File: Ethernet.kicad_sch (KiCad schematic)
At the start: 37 parts, among them J15 RJ45_Hanrun_HR911105A_Horizon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, U7 LAN8720AI-CP-TR, X3 XL2EL89CSI-111YLC-25M

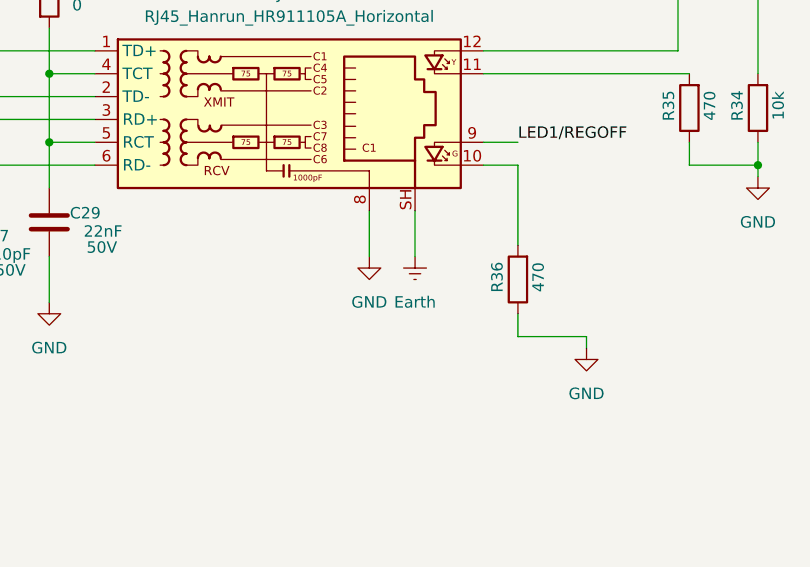
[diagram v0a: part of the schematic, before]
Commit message: Key CHanges for connector choices , termination and semi-final decisions on them
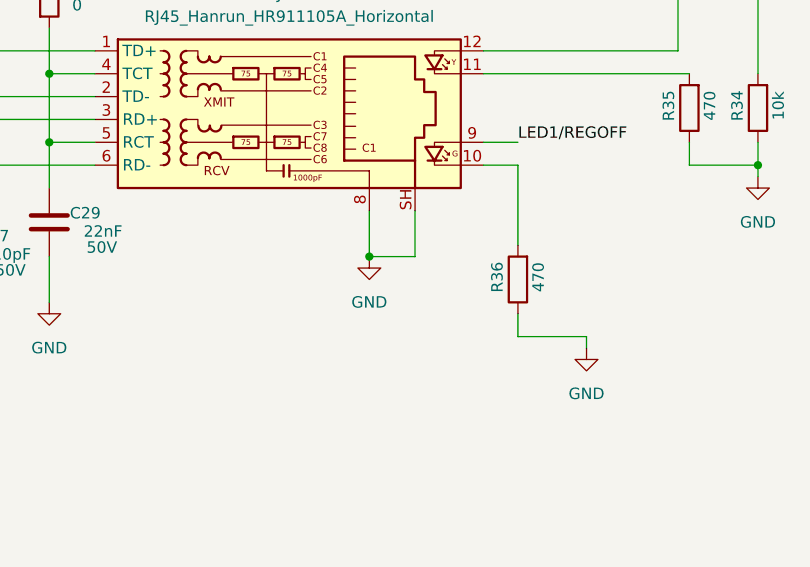
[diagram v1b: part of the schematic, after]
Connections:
- net Earth is gone; now on net GND: J15.SH
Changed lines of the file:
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@@
 	)
 	(junction
+		(at 213.36 60.96)
+		(diameter 0)
+		(color 0 0 0 0)
+	)
+	(junction
 		(at 167.64 16.51)
 		(diameter 0)
@@
 	(wire
 		(pts
+			(xy 213.36 60.96) (xy 218.44 60.96)
+		)
+		(stroke
+			(width 0)
+			(type default)
+		)
+	)
+	(wire
+		(pts
 			(xy 106.68 114.3) (xy 123.19 114.3)
 		)
@@
 					(unit 1)
 				)
-			)
-		)
-	)
-	(symbol
-		(lib_id "power:Earth")
-		(at 218.44 60.96 0)
-		(mirror y)
-		(unit 1)
-		(exclude_from_sim no)
-		(in_bom yes)
-		(on_board yes)
-		(dnp no)
-		(fields_autoplaced yes)
-		(property "Reference" "#PWR069"
-			(at 218.44 67.31 0)
-			(effects
-				(font
-					(size 1.27 1.27)
-				)
-				(hide yes)
-			)
-		)
-		(property "Value" "Earth"
-			(at 218.44 66.04 0)
-			(effects
-				(font
-					(size 1.27 1.27)
-				)
-			)
-		)
-		(property "Footprint" ""
-			(at 218.44 60.96 0)
-			(effects
-				(font
-					(size 1.27 1.27)
-				)
-				(hide yes)
-			)
-		)
-		(property "Datasheet" "~"
-			(at 218.44 60.96 0)
-			(effects
-				(font
-					(size 1.27 1.27)
-				)
-				(hide yes)
-			)
-		)
-		(property "Description" "Power symbol creates a global label with name \"Earth\""
-			(at 218.44 60.96 0)
-			(effects
-				(font
-					(size 1.27 1.27)
-				)
-				(hide yes)
-			)
-		)
-		(pin "1"
-		)
-		(instances
-			(project "OhWare"
-				(path "/38f33acd-ac87-4918-9c1f-d78977d10c9f/1b2d3628-7dd5-4965-8835-e6d8bef60db4"
-					(reference "#PWR069")
-					(unit 1)
-				)

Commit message: Done routing for Buck Converter , Rs485 and CAN , Some Routing for MCU and associated circuitry , NO ETHERNET ROUTING , NO module Interconnects yet
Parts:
- J15: footprint Connector_RJ:RJ45_Hanrun_HR911105A_Horizontal -> EasyEDA:RJ45_Hanrun_HR911105A_Horizontal
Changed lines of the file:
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@@
 			)
 		)
-		(property "Footprint" "Connector_RJ:RJ45_Hanrun_HR911105A_Horizontal"
+		(property "Footprint" "EasyEDA:RJ45_Hanrun_HR911105A_Horizontal"
 			(at 203.2 33.02 0)
 			(effects
